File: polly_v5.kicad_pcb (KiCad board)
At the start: 2 copper layers, 68.6 x 53.3 mm, 40 parts, among them J5 Conn_02x06_Odd_Even, P1 Power, P2 Analog, P3 Digital, P4 Digital, P5 CONN_01X01, P6 CONN_01X01, P7 CONN_01X01, P8 CONN_01X01, U1 4051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

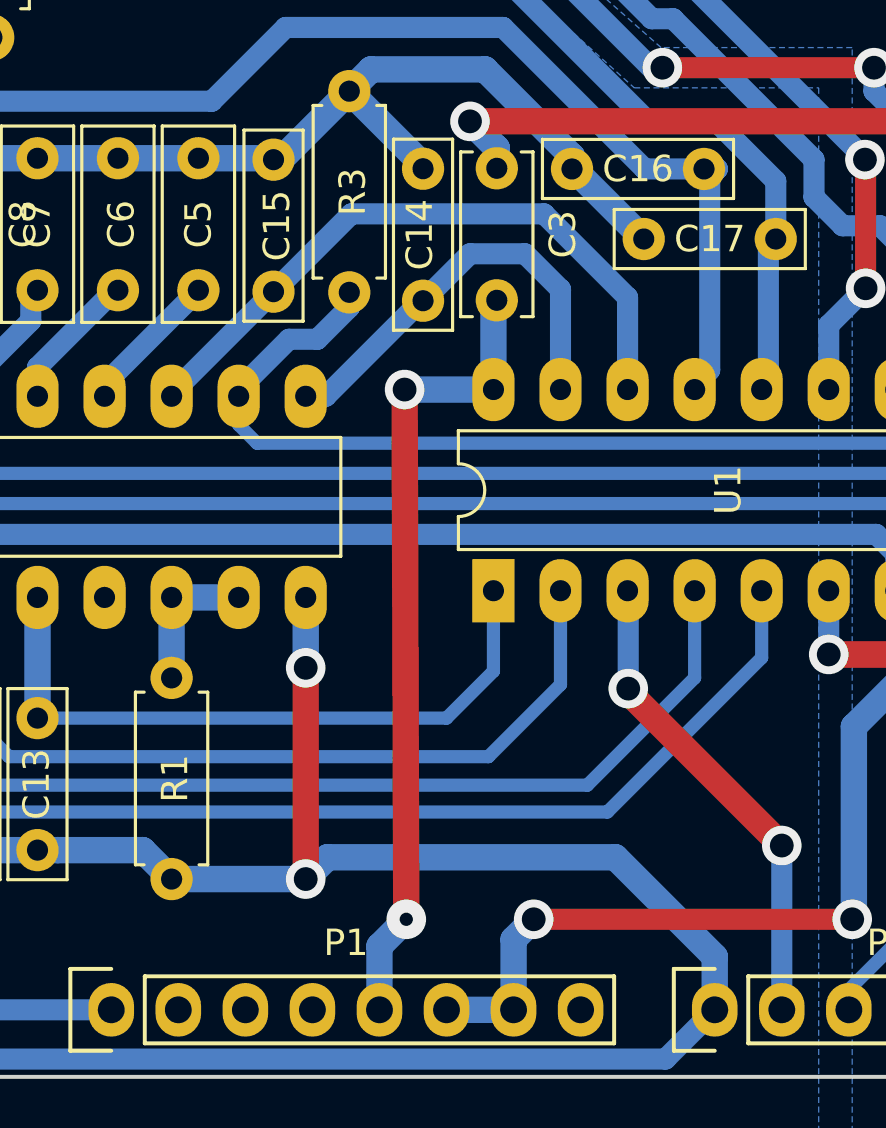
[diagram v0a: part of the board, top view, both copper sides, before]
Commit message: Imporove layout for single sided, add previous versions
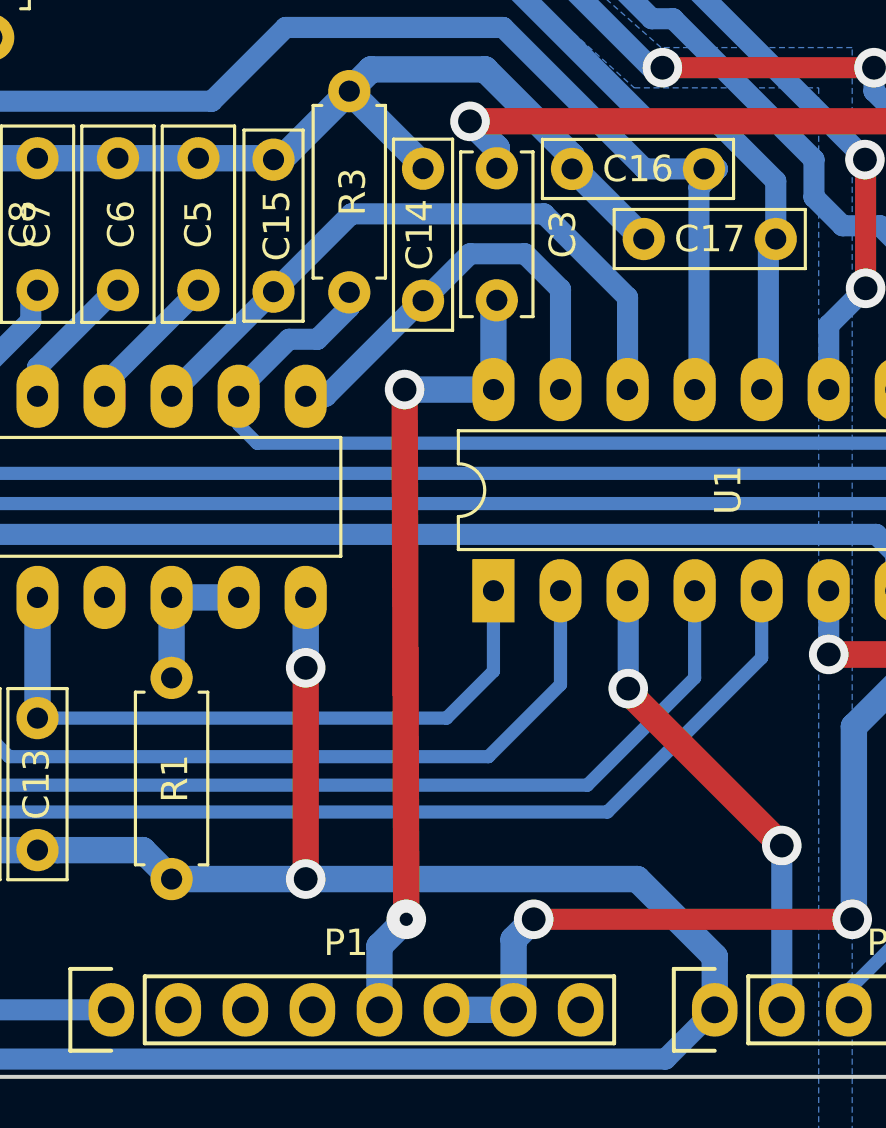
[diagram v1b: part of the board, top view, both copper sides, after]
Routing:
- net GNDA: track 234.5 -> 233.9 mm
